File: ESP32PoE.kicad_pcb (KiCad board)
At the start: 4 copper layers, 90 x 40 mm, 56 parts, among them J1 Conn_01x20_Pin, J2 Conn_01x20_Pin, J3 Conn_01x04_Pin, SW1 SW_Push, SW2 SW_Push, U1 W5500, U2 MagJack-A70-112-331N126, U3 AMS1117-3.3, U4 ESP32-S3-WROOM-1, U7 AG9905LP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

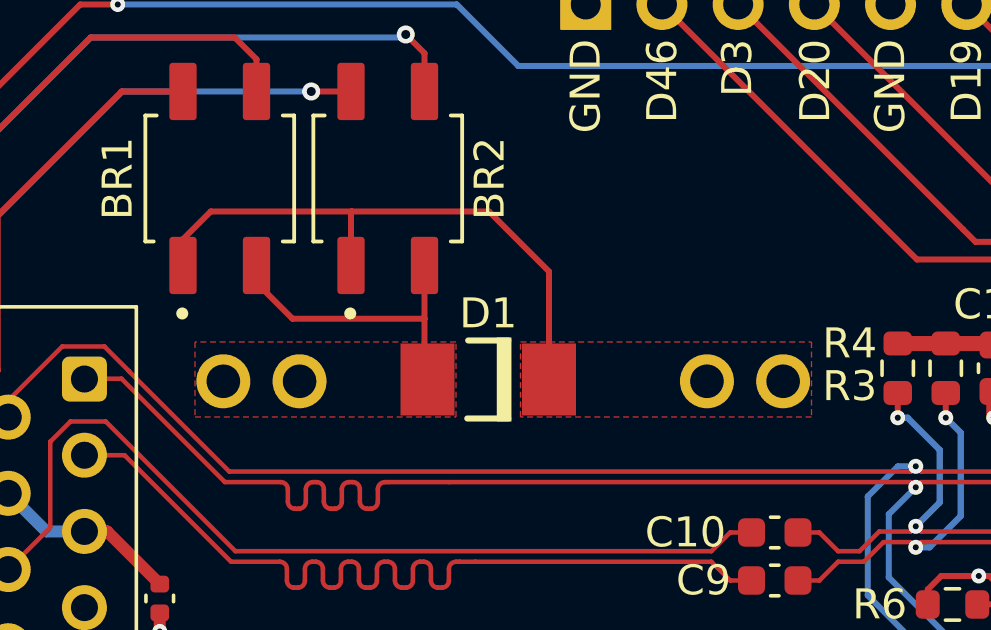
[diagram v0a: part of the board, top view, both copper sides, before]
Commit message: fix: pin order
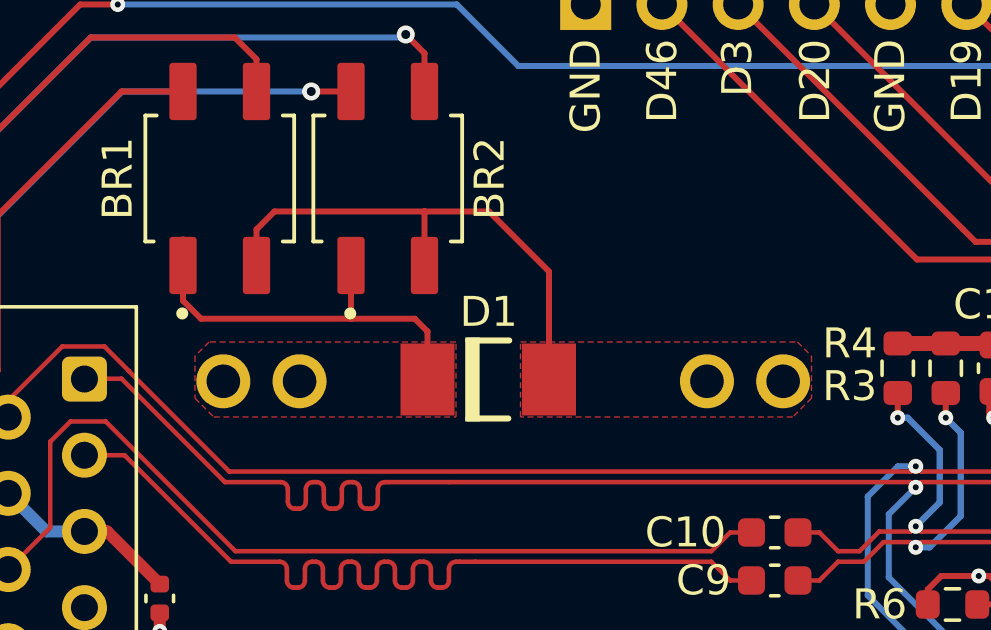
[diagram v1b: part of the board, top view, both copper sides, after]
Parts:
- turned D1 to 0 degrees
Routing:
- net Net-(BR1--): track 10.6 -> 18.0 mm
- net Net-(BR1-+): track 19.7 -> 14.2 mm
